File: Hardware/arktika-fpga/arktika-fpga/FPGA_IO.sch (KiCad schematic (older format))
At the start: 13 parts

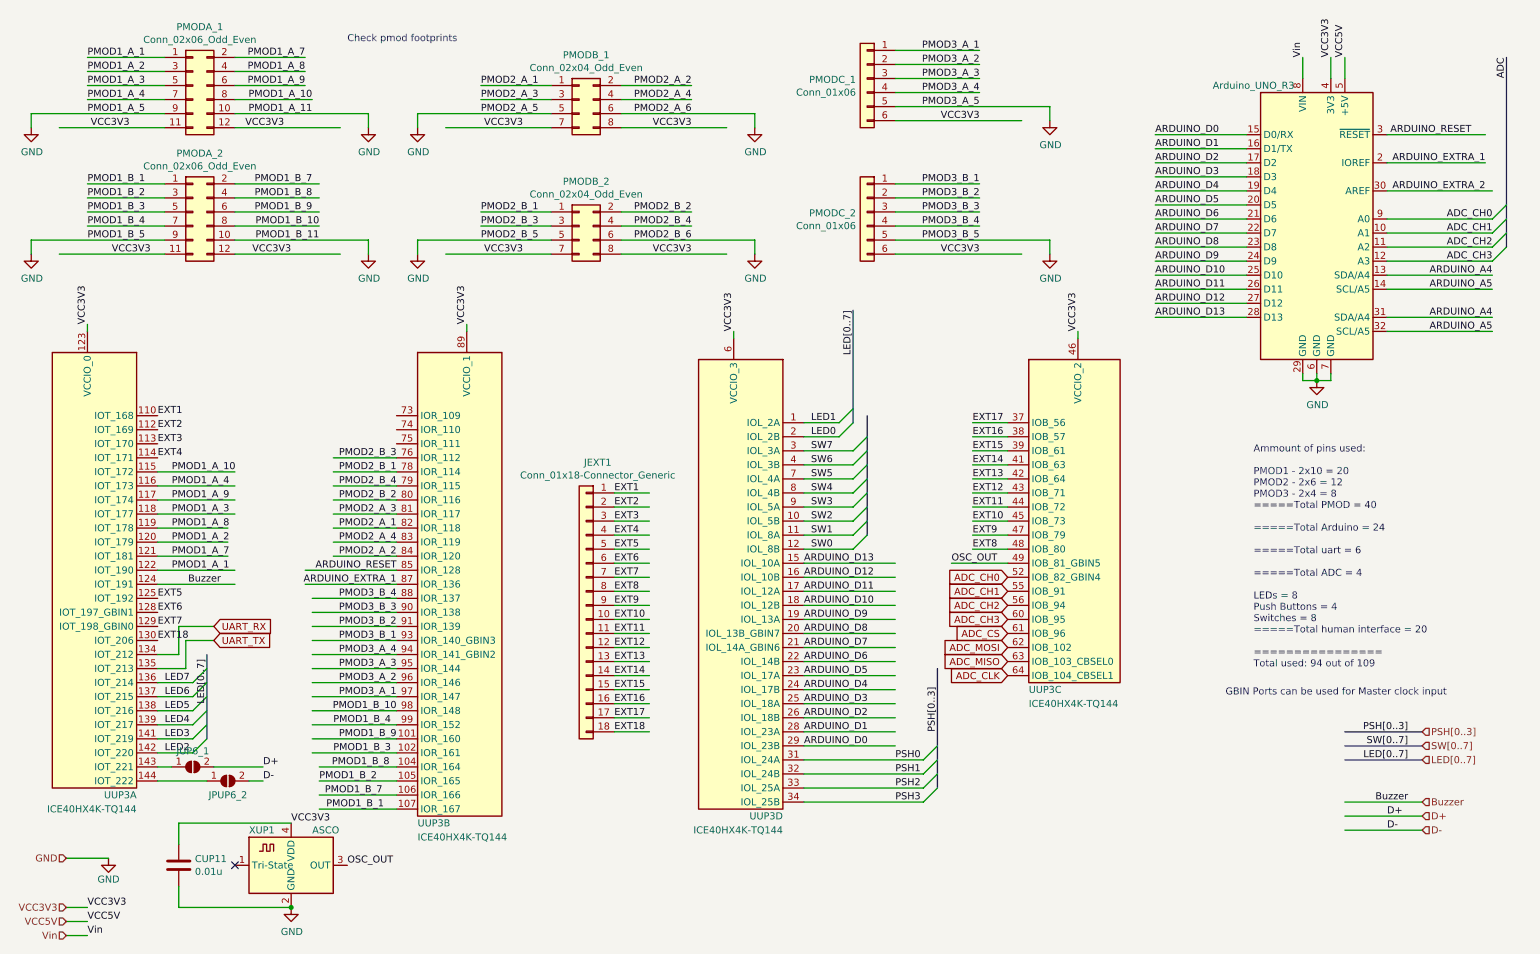
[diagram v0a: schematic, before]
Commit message: Finished routing, did gnd planes, added more silkscreen and some manual via stitching. Pre-final layout.
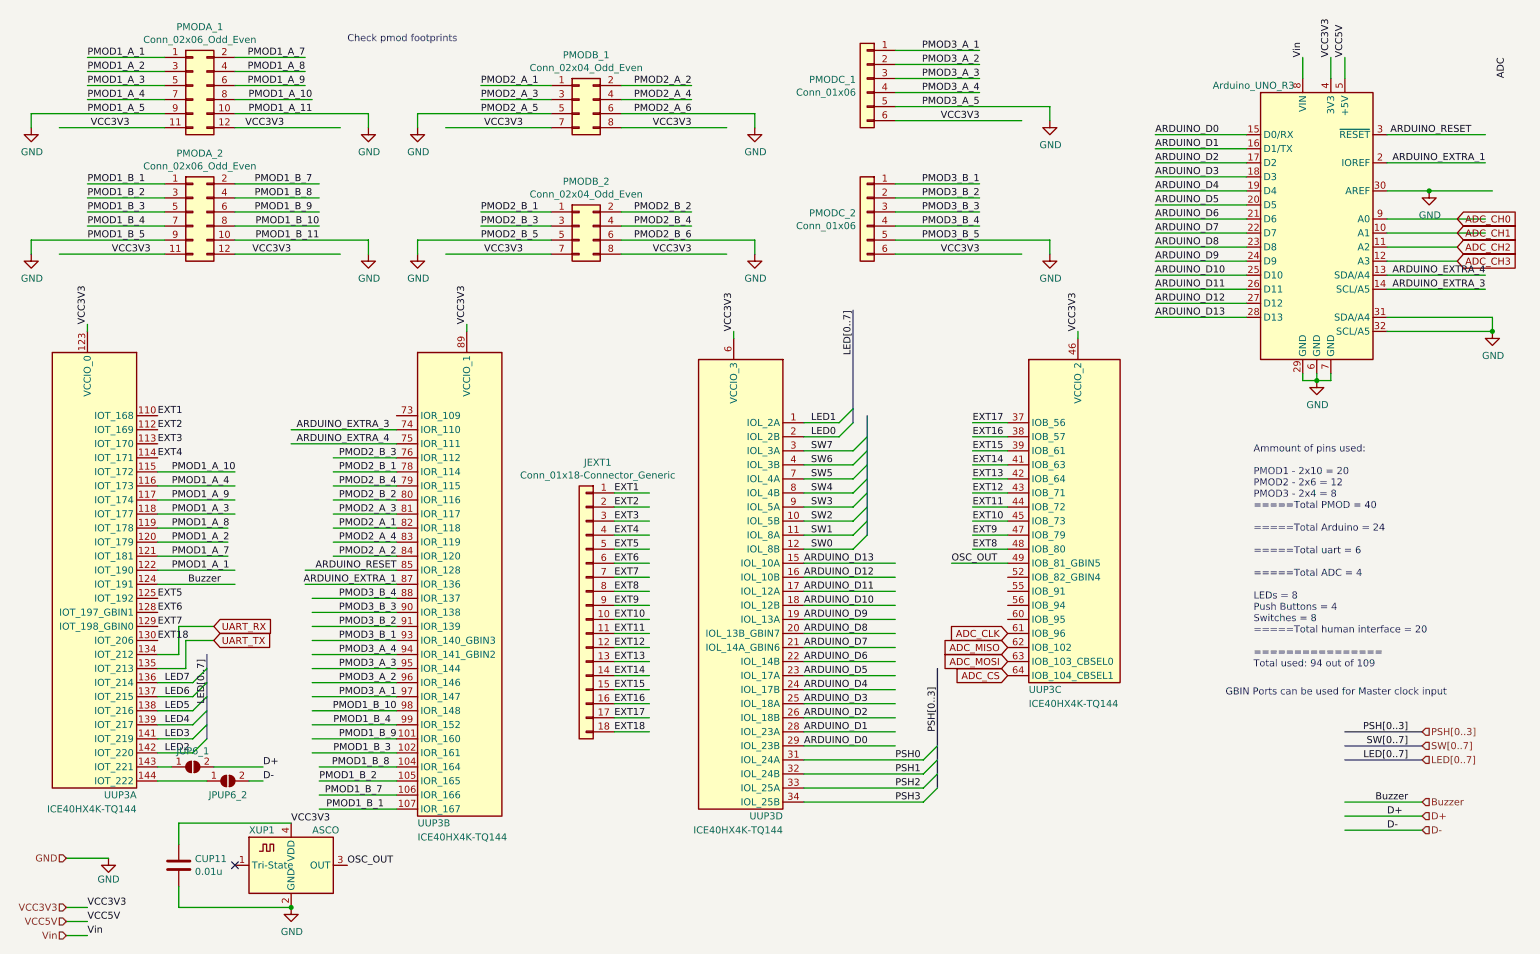
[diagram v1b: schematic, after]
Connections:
- net labels added: ARDUINO_EXTRA_3, ARDUINO_EXTRA_4
- net labels removed: ARDUINO_A4, ARDUINO_A5, ARDUINO_EXTRA_2
- wire segments 218 -> 222
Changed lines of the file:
@@
 Text Label 8650 2650 0    50   ~ 0
 ARDUINO_D13
-Text Label 11050 2350 2    50   ~ 0
-ARDUINO_A4
-Text Label 11050 2450 2    50   ~ 0
-ARDUINO_A5
-Text Label 11050 2650 2    50   ~ 0
-ARDUINO_A4
-Text Label 11050 2750 2    50   ~ 0
-ARDUINO_A5
+Text Label 11000 2450 2    50   ~ 0
+ARDUINO_EXTRA_3
+Text Label 11000 2350 2    50   ~ 0
+ARDUINO_EXTRA_4
 Text Label 11000 1550 2    50   ~ 0
 ARDUINO_EXTRA_1
-Text Label 11000 1750 2    50   ~ 0
-ARDUINO_EXTRA_2
 Wire Wire Line
 	9700 3050 9700 3100
@@
 	9300 2650 8650 2650
 Wire Wire Line
-	10300 1750 11050 1750
-Wire Wire Line
-	11050 2350 10300 2350
-Wire Wire Line
-	10300 2450 11050 2450
+	10300 1750 10600 1750
 Wire Wire Line
 	11050 2650 10300 2650
@@
 OSC_OUT
 NoConn ~ 2100 6550
-Entry Wire Line
-	11050 2250 11150 2150
-Entry Wire Line
-	11050 2150 11150 2050
-Entry Wire Line
-	11050 2050 11150 1950
-Entry Wire Line
-	11050 1950 11150 1850
-Text Label 11050 1950 2    50   ~ 0
-ADC_CH0
-Text Label 11050 2050 2    50   ~ 0
-ADC_CH1
-Text Label 11050 2150 2    50   ~ 0
-ADC_CH2
-Text Label 11050 2250 2    50   ~ 0
-ADC_CH3
 Text Label 11150 800  3    50   ~ 0
 ADC
-Wire Wire Line
-	10300 1950 11050 1950
-Wire Wire Line
-	10300 2050 11050 2050
-Wire Wire Line
-	10300 2150 11050 2150
-Wire Wire Line
-	10300 2250 11050 2250
 Wire Wire Line
 	10300 1550 11000 1550
@@
 Text Label 1600 5750 0    50   ~ 0
 LED2
+Text GLabel 7600 4900 0    50   Input ~ 0
+ADC_CLK
+Text GLabel 7600 5000 0    50   Input ~ 0
+ADC_MISO
+Text GLabel 7600 5100 0    50   Input ~ 0
+ADC_MOSI
 Text GLabel 7600 5200 0    50   Input ~ 0
-ADC_CLK
-Text GLabel 7600 5100 0    50   Input ~ 0
-ADC_MISO
-Text GLabel 7600 5000 0    50   Input ~ 0
-ADC_MOSI
-Text GLabel 7600 4900 0    50   Input ~ 0
 ADC_CS
-Text GLabel 7600 4500 0    50   Input ~ 0
-ADC_CH0
-Text GLabel 7600 4600 0    50   Input ~ 0
-ADC_CH1
-Text GLabel 7600 4700 0    50   Input ~ 0
-ADC_CH2
-Text GLabel 7600 4800 0    50   Input ~ 0
-ADC_CH3
 Text GLabel 1950 4850 2    50   Input ~ 0
 UART_RX
@@
 Wire Wire Line
 	5050 5600 4800 5600
+Text GLabel 10800 1950 2    50   Input ~ 0
+ADC_CH0
+Text GLabel 10800 2050 2    50   Input ~ 0
+ADC_CH1
+Text GLabel 10800 2150 2    50   Input ~ 0
+ADC_CH2
+Text GLabel 10800 2250 2    50   Input ~ 0
+ADC_CH3
+Wire Wire Line
+	10800 2250 10300 2250
+Wire Wire Line
+	10300 2150 10800 2150
+Wire Wire Line
+	10300 1950 11000 1950
+Wire Wire Line
+	10300 2050 11000 2050
+Text Label 3200 3450 2    50   ~ 0
+ARDUINO_EXTRA_3
+Text Label 3200 3550 2    50   ~ 0
+ARDUINO_EXTRA_4
+Wire Wire Line
+	2500 3450 3250 3450
+Wire Wire Line
+	2500 3550 3250 3550
+Wire Wire Line
+	10300 2350 11000 2350
+Wire Wire Line
+	10300 2450 11000 2450
+$Comp
+L arktika-fpga-rescue:GND-power #PWR0161
+U 1 1 5FD857D0
+P 11050 2750
+F 0 "#PWR0161" H 11050 2500 50  0001 C CNN
+F 1 "GND" H 11055 2577 50  0000 C CNN
+F 2 "" H 11050 2750 50  0001 C CNN
+F 3 "" H 11050 2750 50  0001 C CNN
+	1    11050 2750
+	1    0    0    -1
+$EndComp
+Wire Wire Line
+	11050 2650 11050 2750
 Wire Bus Line
 	6500 2600 6500 3400
@@
 	7100 5150 7100 6000
 Wire Bus Line
-	11150 800  11150 2150
-Wire Bus Line
 	1900 5050 1900 5650
 Wire Bus Line
 	6600 3350 6600 4200
+Connection ~ 11050 2750
+$Comp
+L arktika-fpga-rescue:GND-power #PWR0162
+U 1 1 5FD9ECAC
+P 10600 1750
+F 0 "#PWR0162" H 10600 1500 50  0001 C CNN
+F 1 "GND" H 10605 1577 50  0000 C CNN
+F 2 "" H 10600 1750 50  0001 C CNN
+F 3 "" H 10600 1750 50  0001 C CNN
+	1    10600 1750
+	1    0    0    -1
+$EndComp
+Connection ~ 10600 1750
+Wire Wire Line
+	10600 1750 11050 1750
 $EndSCHEMATC

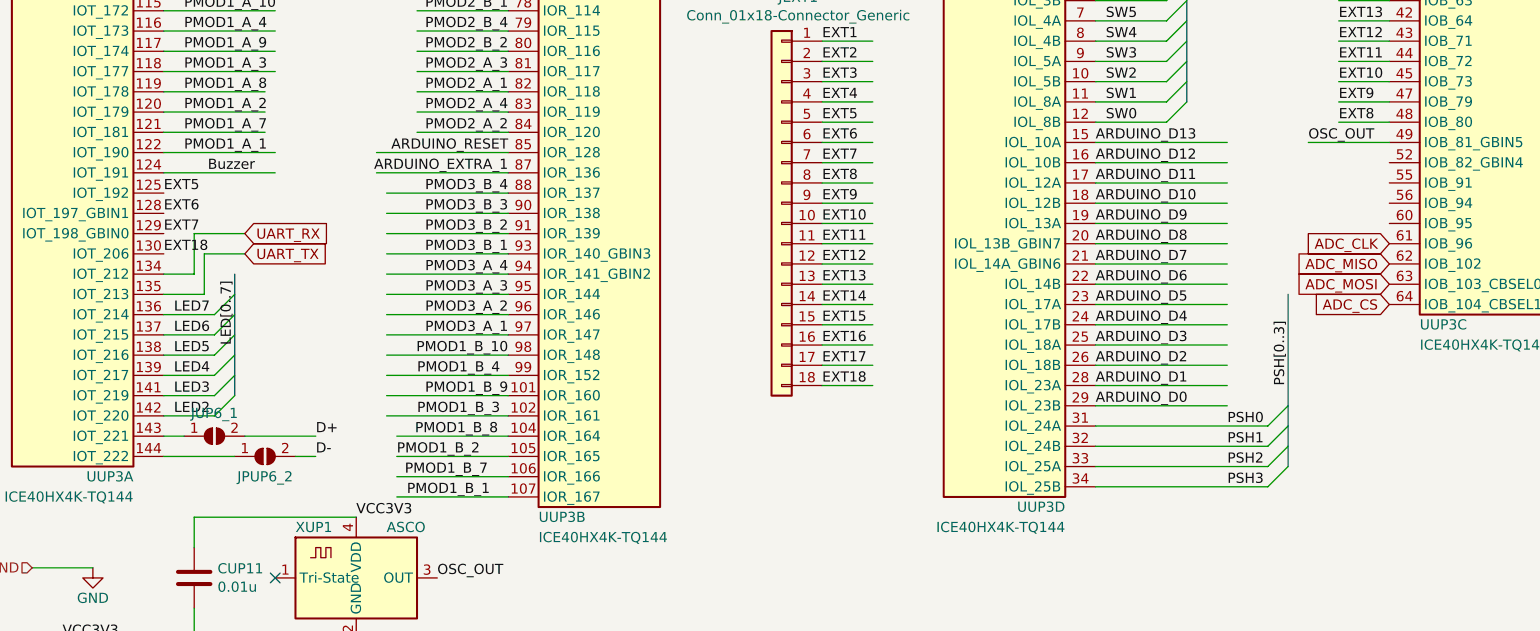
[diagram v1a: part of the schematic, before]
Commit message: Fixed minor drc errors. removed usb jumpers and added needed resistors
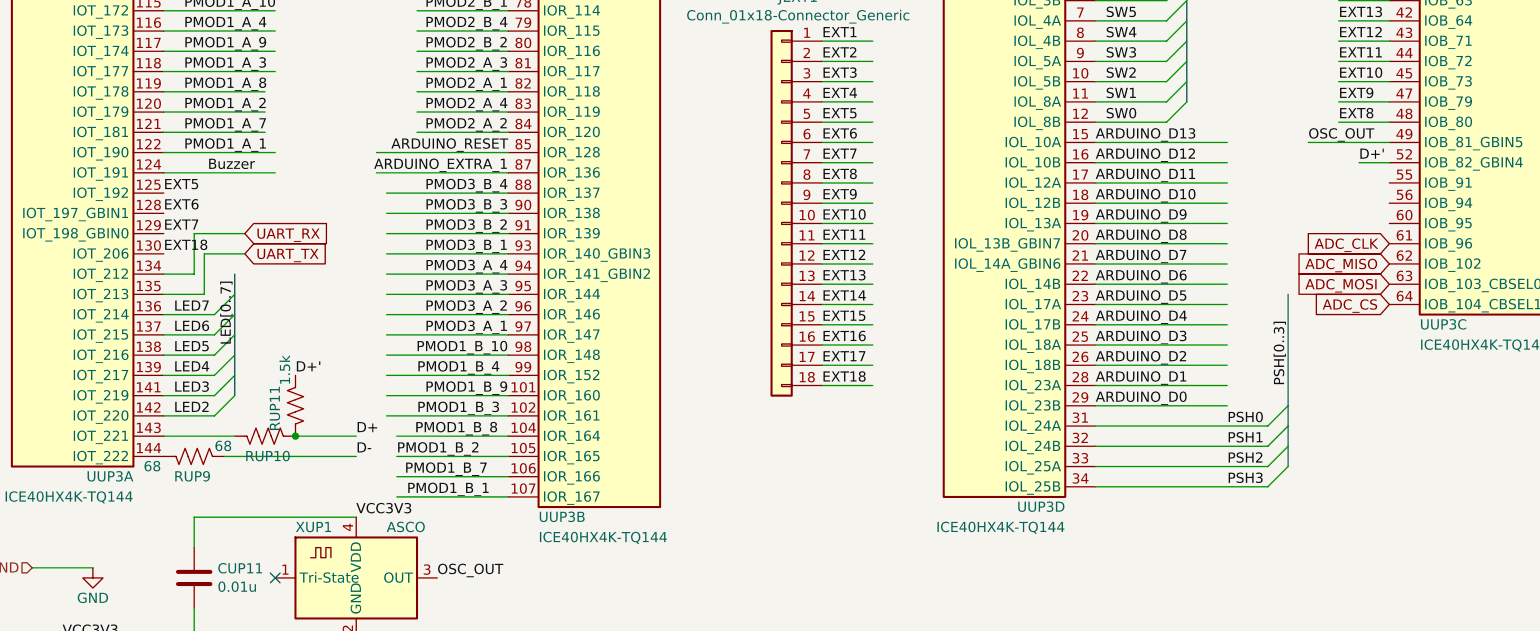
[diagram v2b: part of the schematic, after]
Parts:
- removed JPUP6_2, JUP6_1: SolderJumper_2_Open, Jumper:SolderJumper-2_P1.3mm_Open_RoundedPad1.0x1.5mm, symbol Jumper:SolderJumper_2_Open
- added RUP10, RUP9: 68, Resistor_SMD:R_0603_1608Metric_Pad1.05x0.95mm_HandSolder, symbol arktika-fpga-rescue:R_US-Device
- added RUP11: 1.5k, Resistor_SMD:R_0603_1608Metric_Pad1.05x0.95mm_HandSolder, symbol arktika-fpga-rescue:R_US-Device
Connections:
- net labels added: D+'
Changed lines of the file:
@@
 Text Label 10300 6300 0    50   ~ 0
 D-
-Text Label 2300 5850 0    50   ~ 0
+Text Label 2500 5850 0    50   ~ 0
 D+
-Text Label 2300 5950 0    50   ~ 0
+Text Label 2500 5950 0    50   ~ 0
 D-
-$Comp
-L Jumper:SolderJumper_2_Open JUP6_1
-U 1 1 5F315AF6
-P 1800 5850
-F 0 "JUP6_1" H 1800 5963 50  0000 C CNN
-F 1 "SolderJumper_2_Open" H 1800 5964 50  0001 C CNN
-F 2 "Jumper:SolderJumper-2_P1.3mm_Open_RoundedPad1.0x1.5mm" H 1800 5850 50  0001 C CNN
-F 3 "~" H 1800 5850 50  0001 C CNN
-	1    1800 5850
-	1    0    0    -1
-$EndComp
-$Comp
-L Jumper:SolderJumper_2_Open JPUP6_2
-U 1 1 5F3163BA
-P 2050 5950
-F 0 "JPUP6_2" H 2050 5850 50  0000 C CNN
-F 1 "SolderJumper_2_Open" H 2050 6064 50  0001 C CNN
-F 2 "Jumper:SolderJumper-2_P1.3mm_Open_RoundedPad1.0x1.5mm" H 2050 5950 50  0001 C CNN
-F 3 "~" H 2050 5950 50  0001 C CNN
-	1    2050 5950
-	1    0    0    -1
-$EndComp
-Wire Wire Line
-	1550 5850 1650 5850
-Wire Wire Line
-	1550 5950 1900 5950
-Wire Wire Line
-	1950 5850 2300 5850
-Wire Wire Line
-	2300 5950 2200 5950
 Text Label 3250 4150 2    50   ~ 0
 PMOD2_A_1
@@
 Wire Wire Line
 	11050 2650 11050 2750
-Wire Bus Line
-	6500 2600 6500 3400
-Wire Bus Line
-	7100 5150 7100 6000
-Wire Bus Line
-	1900 5050 1900 5650
-Wire Bus Line
-	6600 3350 6600 4200
 Connection ~ 11050 2750
 $Comp
@@
 Wire Wire Line
 	10600 1750 11050 1750
+$Comp
+L arktika-fpga-rescue:R_US-Device R?
+U 1 1 5FEAB72B
+P 2050 5850
+AR Path="/5FEAB72B" Ref="R?"  Part="1"
+AR Path="/5F3E98C5/5FEAB72B" Ref="R?"  Part="1"
+AR Path="/5F415705/5FEAB72B" Ref="R?"  Part="1"
+AR Path="/5F516611/5FEAB72B" Ref="RUP10"  Part="1"
+F 0 "RUP10" V 2150 5950 50  0000 R CNN
+F 1 "68" V 2100 6100 50  0000 R CNN
+F 2 "Resistor_SMD:R_0603_1608Metric_Pad1.05x0.95mm_HandSolder" V 2090 5840 50  0001 C CNN
+F 3 "~" H 2050 5850 50  0001 C CNN
+	1    2050 5850
+	0    -1   1    0
+$EndComp
+$Comp
+L arktika-fpga-rescue:R_US-Device R?
+U 1 1 5FEC2363
+P 1700 5950
+AR Path="/5FEC2363" Ref="R?"  Part="1"
+AR Path="/5F3E98C5/5FEC2363" Ref="R?"  Part="1"
+AR Path="/5F415705/5FEC2363" Ref="R?"  Part="1"
+AR Path="/5F516611/5FEC2363" Ref="RUP9"  Part="1"
+F 0 "RUP9" V 1800 6050 50  0000 R CNN
+F 1 "68" V 1750 6200 50  0000 R CNN
+F 2 "Resistor_SMD:R_0603_1608Metric_Pad1.05x0.95mm_HandSolder" V 1740 5940 50  0001 C CNN
+F 3 "~" H 1700 5950 50  0001 C CNN
+	1    1700 5950
+	0    -1   1    0
+$EndComp
+Wire Wire Line
+	1550 5850 1900 5850
+$Comp
+L arktika-fpga-rescue:R_US-Device R?
+U 1 1 5FF05F9F
+P 2200 5700
+AR Path="/5FF05F9F" Ref="R?"  Part="1"
+AR Path="/5F3E98C5/5FF05F9F" Ref="R?"  Part="1"
+AR Path="/5F415705/5FF05F9F" Ref="R?"  Part="1"
+AR Path="/5F516611/5FF05F9F" Ref="RUP11"  Part="1"
+F 0 "RUP11" V 2300 5800 50  0000 R CNN
+F 1 "1.5k" V 2250 5950 50  0000 R CNN
+F 2 "Resistor_SMD:R_0603_1608Metric_Pad1.05x0.95mm_HandSolder" V 2240 5690 50  0001 C CNN
+F 3 "~" H 2200 5700 50  0001 C CNN
+	1    2200 5700
+	-1   0    0    -1
+$EndComp
+Text Label 2200 5550 0    50   ~ 0
+D+'
+Text Label 7450 4500 0    50   ~ 0
+D+'
+Wire Wire Line
+	7450 4500 7600 4500
+Wire Wire Line
+	2200 5850 2500 5850
+Connection ~ 2200 5850
+Wire Wire Line
+	1850 5950 2500 5950
+Wire Bus Line
+	6500 2600 6500 3400
+Wire Bus Line
+	7100 5150 7100 6000
+Wire Bus Line
+	1900 5050 1900 5650
+Wire Bus Line
+	6600 3350 6600 4200
 $EndSCHEMATC

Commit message: Exported final gerbers. Sent to fab
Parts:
- XUP1: footprint Arktica-Specific:Crystal_SMD_7050-4pin_7.0x5.0mm_MOD_3225 -> Crystals:Crystal_SMD_3225-4pin_3.2x2.5mm_HandSoldering
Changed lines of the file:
@@
 F 0 "XUP1" H 2200 6800 50  0000 L CNN
 F 1 "ASCO" H 2650 6800 50  0000 L CNN
-F 2 "Arktica-Specific:Crystal_SMD_7050-4pin_7.0x5.0mm_MOD_3225" H 2600 6200 50  0001 C CNN
+F 2 "Crystals:Crystal_SMD_3225-4pin_3.2x2.5mm_HandSoldering" H 2600 6200 50  0001 C CNN
 F 3 "https://abracon.com/Oscillators/ASCO.pdf" H 2275 6675 50  0001 C CNN
 	1    2500 6550
